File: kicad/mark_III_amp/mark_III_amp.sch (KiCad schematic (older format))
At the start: 112 parts

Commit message: Улучшил входной диф. каскад у Mark III.
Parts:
- removed R35, R37, R38, R39, R42, R43, R44, R45, R46, R47, R48, R49, R50, R51: 1.2, symbol RESISTOR_1W
- removed VD1, VD2, VD3, VD4: SS16, symbol SHOTTKY_DIODE
- added C9: 470 мк 35 В, symbol CAPITORS_ELECTROLYTIC
- added R12, R18: 2.2 к, symbol RESISTOR_0_25W
- added R37, R39, R42, R43, R44, R45: 0.47, symbol RESISTOR_2W
- added VD1, VD2: VS-MBRB20100CTPBF, symbol DIOD_SCHTOTTKY_DUAL
- added VT3, VT7: MMBT5551, symbol MMBT5551
- C10: renamed from C9; value 2.2 мк -> 4.7 мк
- C11: renamed from C10; value 47 п -> 68 п
- C12: renamed from C11; value 47 п -> 68 п
- C4: value 2.2 мк -> 4.7 мк
- C7: value 470 п -> 220 п
- C8: value 220 мк 63 В -> 470 мк 35 В
- R36: renamed from R34; value 1.2 -> 0.47; symbol RESISTOR_1W -> RESISTOR_2W
- R38: renamed from R36; value 1.2 -> 0.47; symbol RESISTOR_1W -> RESISTOR_2W
- R8: value 47 к -> 22 к
- R9: value 470 -> 220
- renumbered C12 to C13, C13 to C14, C14 to C15, C15 to C16, C16 to C17, C17 to C18, C18 to C19, C19 to C20, C20 to C21, C21 to C22, R12 to R13, R13 to R14, R14 to R15, R15 to R16, R16 to R19, R18 to R20, R19 to R21, R20 to R22, R21 to R23, R22 to R24, R23 to R25, R24 to R26, R25 to R27, R26 to R28, R27 to R29, R28 to R30, R29 to R31, R30 to R32, R31 to R33, R32 to R34, R33 to R35, R52 to R46, R53 to R47, R54 to R48, R55 to R49, R56 to R50, R57 to R51, R58 to R52, R59 to R53, VD5 to VD3, VT8 to VT10, VT9 to VT11, VT10 to VT12, VT11 to VT13, VT12 to VT14, VT13 to VT15, VT14 to VT16, VT15 to VT17, VT16 to VT18, VT17 to VT19, VT3 to VT2, VT18 to VT20, VT19 to VT21, VT2 to VT4, VT4 to VT5, VT5 to VT8, VT7 to VT9
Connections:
- net GND: now also C9.1
- net at C7.1, R9.2: now also VT2.1; no longer VT4.2
- net at R16.1, VT2.2: now also VT3.3
- net at R16.3, VT8.2: now also VT7.3
- net at C10.2, C8.2, R11.1: now also C9.2
- net at R11.2, R31.1: now also VT8.1; no longer VT6.2
- net at C11.1, VT10.2, VT4.3: now also R12.1, VT3.1; no longer VT2.3
- net at C20.2, C21.1, L1.2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: now also R37.1, R39.1, R42.2, R43.1, R44.2, R45.1
- net at R36.1, R38.1, VT16.3: now also VD1.1
- net at VT18.3: now also R42.1, R44.1, VD1.3
- net at VT17.3: now also R37.2, R39.2, VD2.3
- net at VT19.3: now also R43.2, R45.2, VD2.1
- net at R46.1: now also VD1.2, VD2.2
- new net: R18.1, VT4.2, VT6.2, VT6.3, VT7.1
- new net: R18.2, VT7.2, VT8.3
- new net: R12.2, VT2.3, VT3.2
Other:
- moved on the sheet: C10, R13, R16, R19, VT2, VT4, VT6, VT8

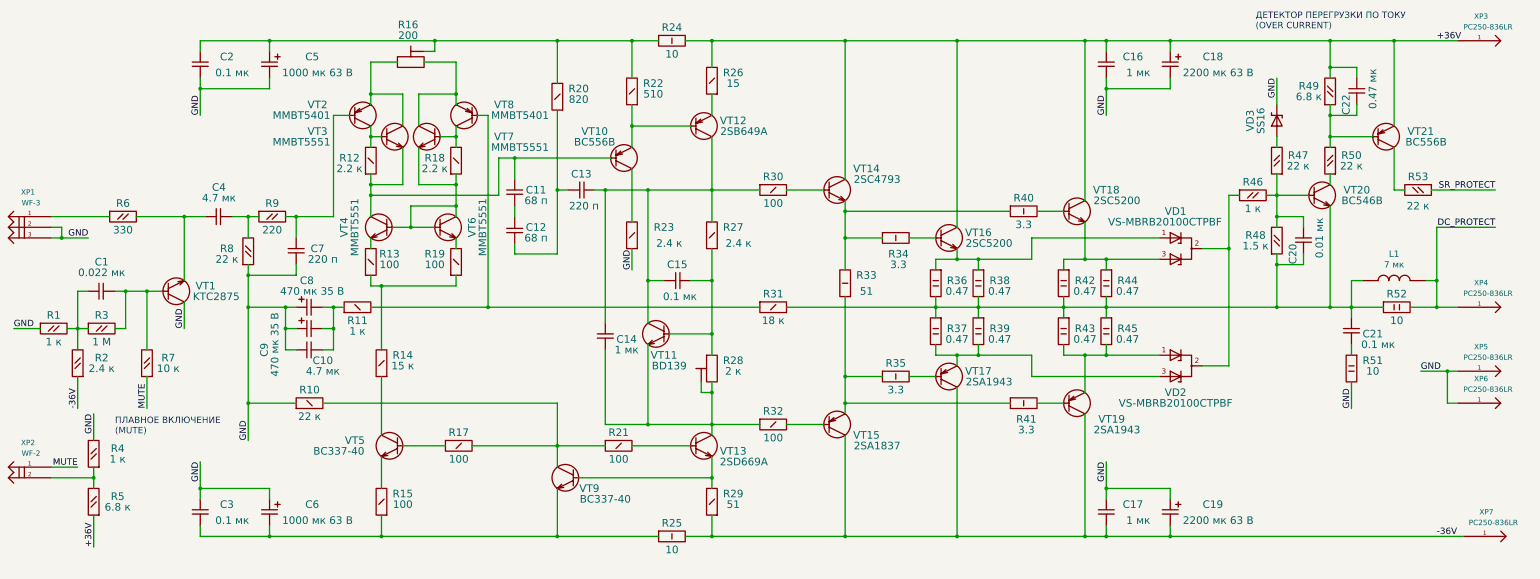
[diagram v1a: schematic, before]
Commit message: Поправил схему усилителя Mark III.
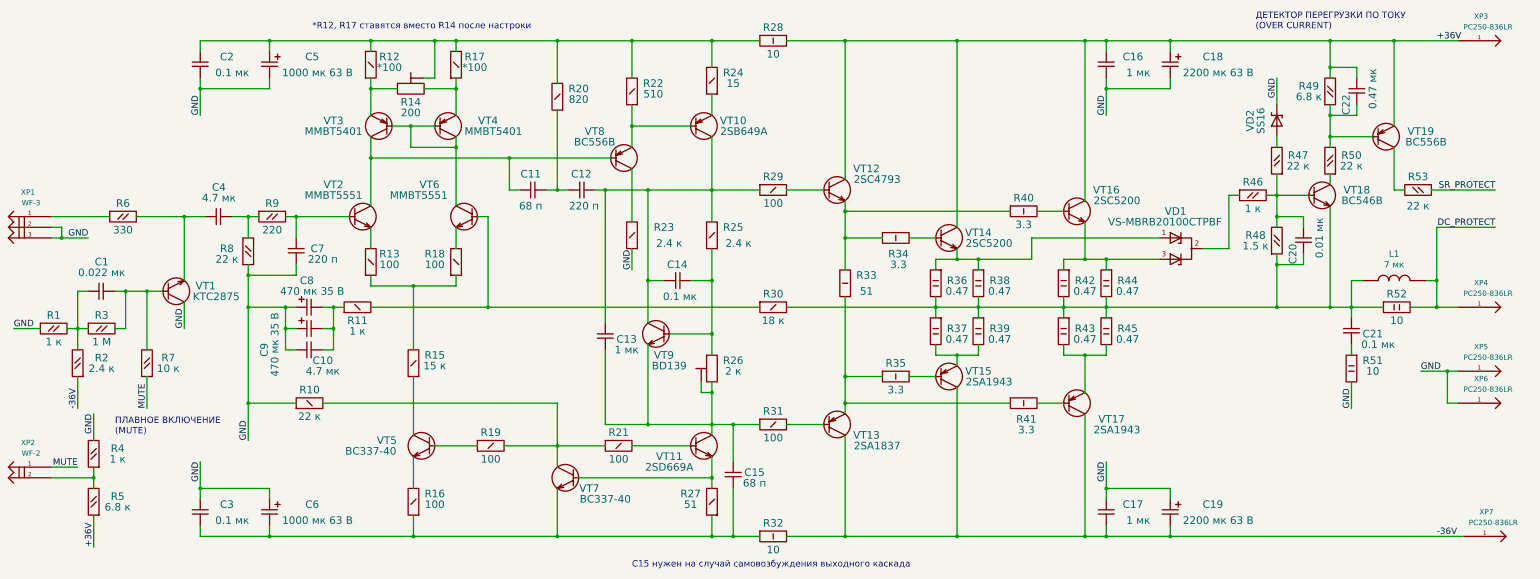
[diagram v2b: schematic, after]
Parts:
- removed C12: 68 п, symbol CAPITORS
- removed R18: 2.2 к, symbol RESISTOR_0_25W
- removed VD2: VS-MBRB20100CTPBF, symbol DIOD_SCHTOTTKY_DUAL
- removed VT2, VT8: MMBT5401, symbol MMBT5401
- removed VT3, VT4, VT7: MMBT5551, symbol MMBT5551
- added C15: 68 п, symbol CAPITORS
- added R17: *100, symbol RESISTOR_0_25W
- added VT2: MMBT5551, symbol MMBT5551
- added VT3, VT4: MMBT5401, symbol MMBT5401
- R12: value 2.2 к -> *100
- renumbered C13 to C12, C14 to C13, C15 to C14, R16 to R14, R14 to R15, R15 to R16, R19 to R18, R17 to R19, R26 to R24, R27 to R25, R28 to R26, R29 to R27, R24 to R28, R30 to R29, R31 to R30, R32 to R31, R25 to R32, VD3 to VD2, VT12 to VT10, VT13 to VT11, VT14 to VT12, VT15 to VT13, VT16 to VT14, VT17 to VT15, VT18 to VT16, VT19 to VT17, VT20 to VT18, VT21 to VT19, VT9 to VT7, VT10 to VT8, VT11 to VT9
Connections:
- net +36V: no longer R24.2
- net -36V: no longer R27.1
- net at C7.1, R9.2: now also VT2.2
- net at R13.2: now also VT2.1
- net at C2.1, C5.1, R14.2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: now also R12.2, R24.2, R17.2
- net at R14.1: now also R12.1, VT3.2
- net at R14.3: now also R17.1, VT4.2
- net at R11.2, R30.1: now also VT6.2
- net at C11.1, VT8.2: now also VT2.3, VT3.3; no longer R12.1
- net at C11.2: now also C12.2, R20.1
- net at C13.2, R26.2, R26.3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: now also C15.1
- net at C3.2, C6.2, R16.1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: now also R27.1, C15.2
- net at VT6.3: now also VT3.1, VT4.1, VT4.3; no longer VT6.2
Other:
- note added: "*R12, R17 ставятся вместо R14 после настроки"
- note added: "C15 нужен на случай самовозбуждения выходного каскада"
- moved on the sheet: C11, R14, R15, R16, R19, R28, R32, VT5
